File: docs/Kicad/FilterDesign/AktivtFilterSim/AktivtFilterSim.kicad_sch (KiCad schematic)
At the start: 10 parts, among them J5 Conn_01x02_Pin, U2 MCP6002-xMC

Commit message: KICAD SIM IS HARD
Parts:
- removed U2: MCP6002-xMC, Package_DFN_QFN:DFN-8-1EP_3x2mm_P0.5mm_EP1.75x1.45mm, symbol Amplifier_Operational:MCP6002-xMC
- added J2: Conn_01x02_Pin, symbol Connector:Conn_01x02_Pin
- added R5: 1M, symbol Device:R
- added U1: TLV9062, symbol Amplifier_Operational:TLV9062
- renumbered C7 to C1, C8 to C2, C9 to C3, C10 to C4, J5 to J1, R9 to R1, R8 to R2, R11 to R3, R10 to R4
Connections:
- net +3.3V: now also U1.8 (V+)
- net GND: now also J2.2 (Pin_2), R5.2, U1.4 (V-); no longer J1.2 (Pin_2)
- net at C4.1, R4.2: now also U1.5 (+)
- net out1: now reaches C1.2, R3.1
- net out1: now also U1.1, U1.2 (-)
- net at C3.1, R2.2: now also U1.3 (+)
- net out2: now reaches C2.2
- net out2: now also J2.1 (Pin_1), U1.6 (-), U1.7
- net in: now reaches J1.1 (Pin_1), R1.1
- new net: J1.2 (Pin_2), R5.1
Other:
- note added: ".tran 10n 2m"
- moved on the sheet: C1, C2, C3, C4, J1, R1, R2, R3, R4

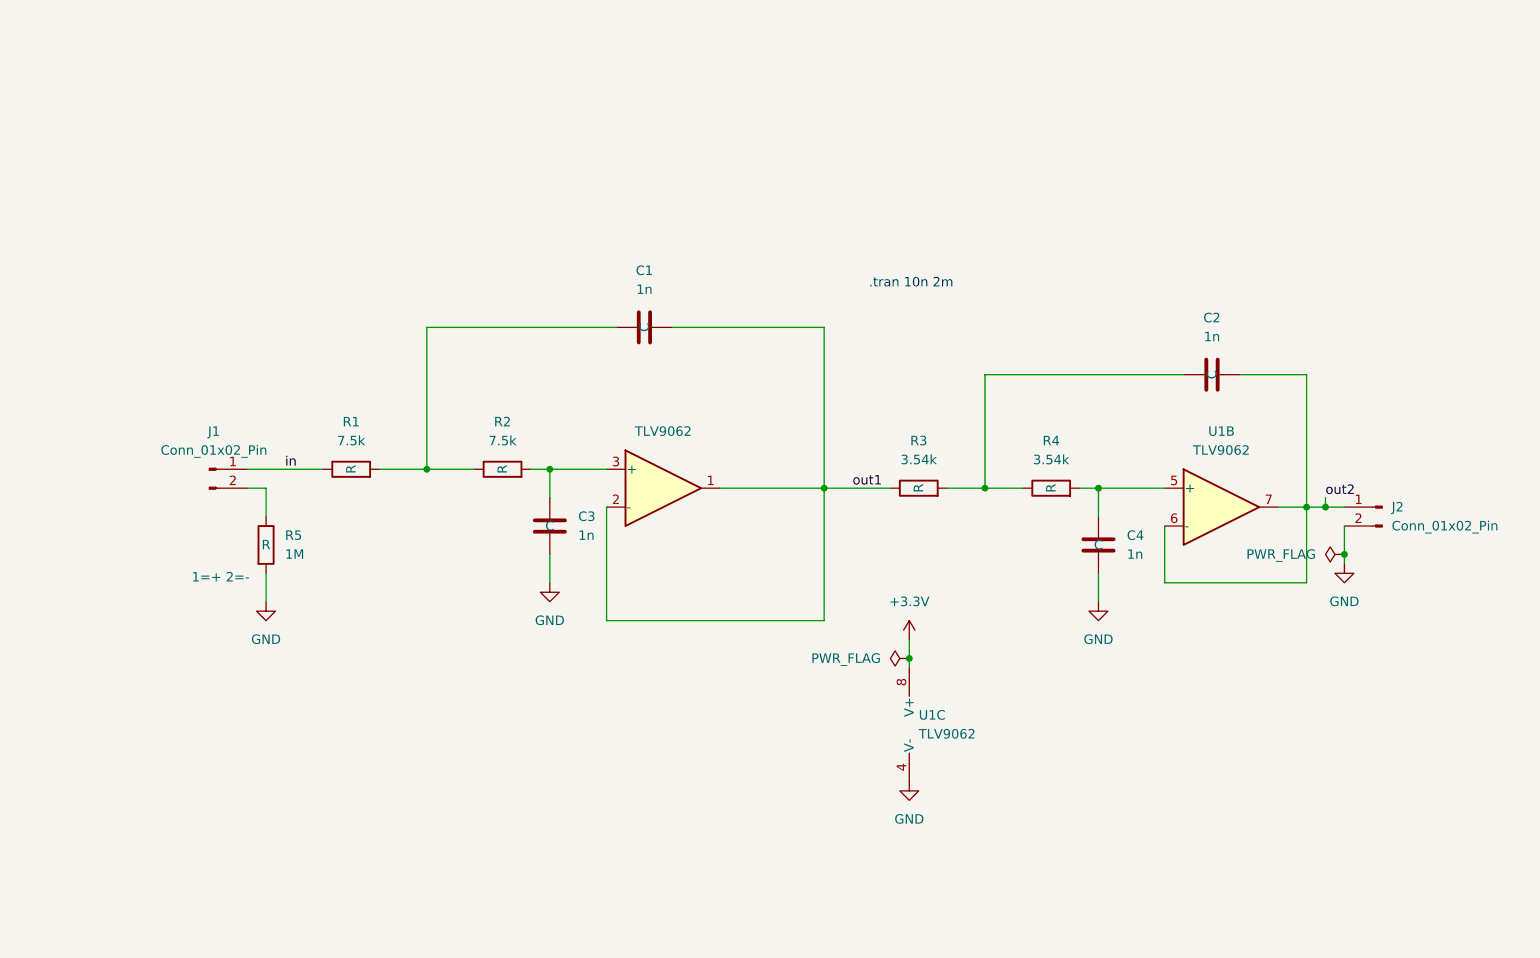
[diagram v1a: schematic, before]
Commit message: Filter with LT1013 having pin assignment issues
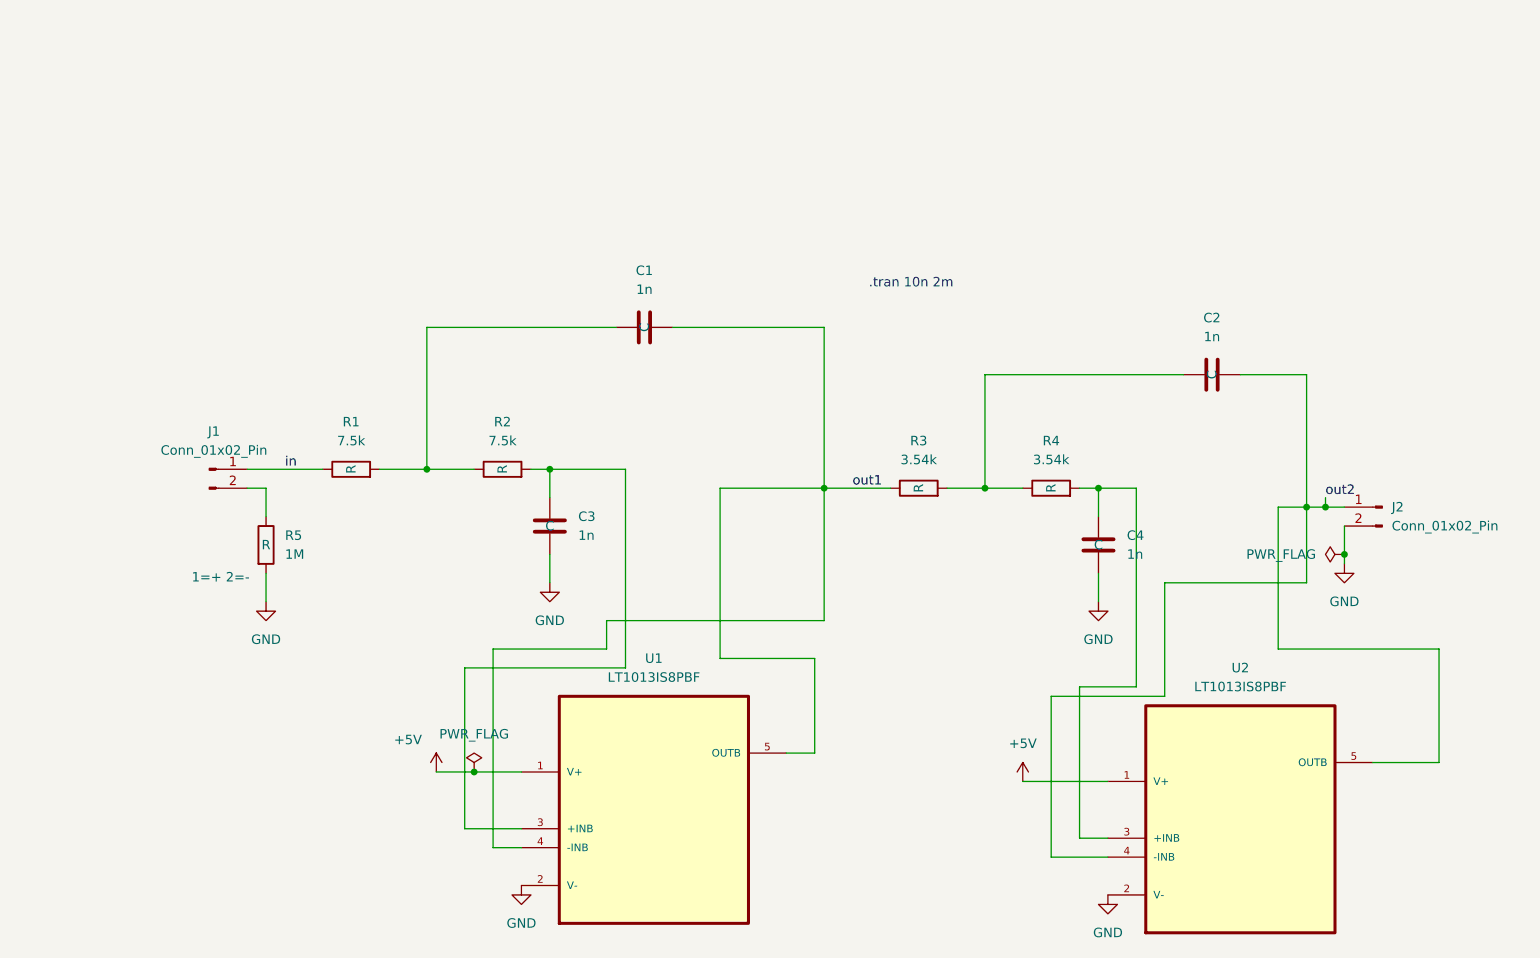
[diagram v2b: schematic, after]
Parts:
- removed U1: TLV9062, symbol Amplifier_Operational:TLV9062
- added U1, U2: LT1013IS8PBF, LT1013IS8PBF:SOIC127P600X175-8N, symbol LT1013IS8PBF:LT1013IS8PBF
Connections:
- net GND: now also U1.2 (V-), U2.2 (V-)
- net out1: now also U1.4 (-INB), U1.5 (OUTB)
- net out2: now also U2.4 (-INB), U2.5 (OUTB)
- net at C4.1, R4.2: now also U2.3 (+INB)
- net at C3.1, R2.2: now also U1.3 (+INB)
- new net +5V: U1.1 (V+), U2.1 (V+)
